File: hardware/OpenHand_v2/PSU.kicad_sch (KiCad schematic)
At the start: 23 parts, among them Q1 AO3401A, U2 TPS565201DDCR, U3 AMS1117-3.3

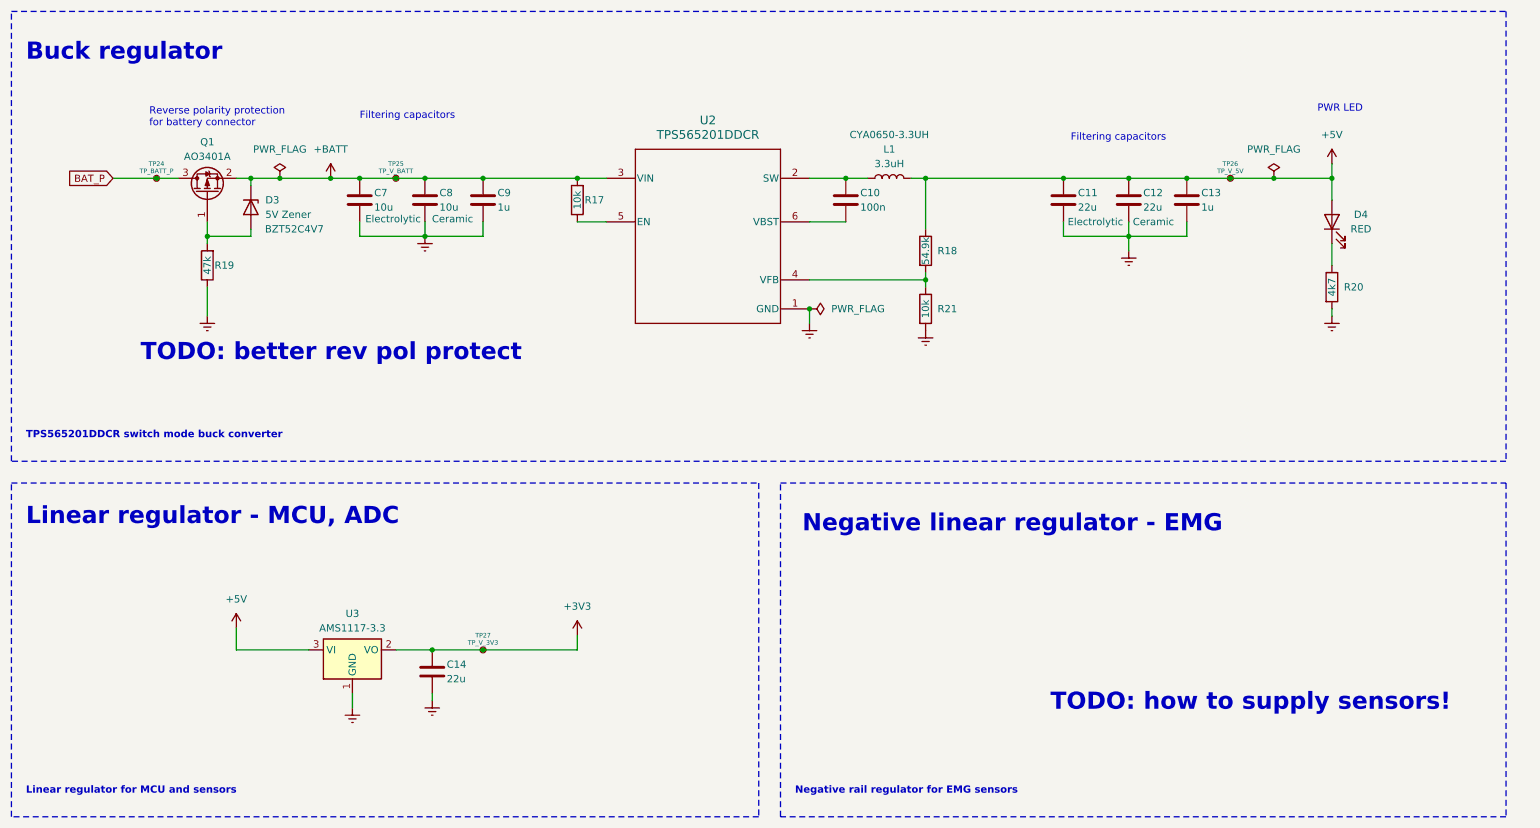
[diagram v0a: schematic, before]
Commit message: Update V2 schematic and start PCB layout
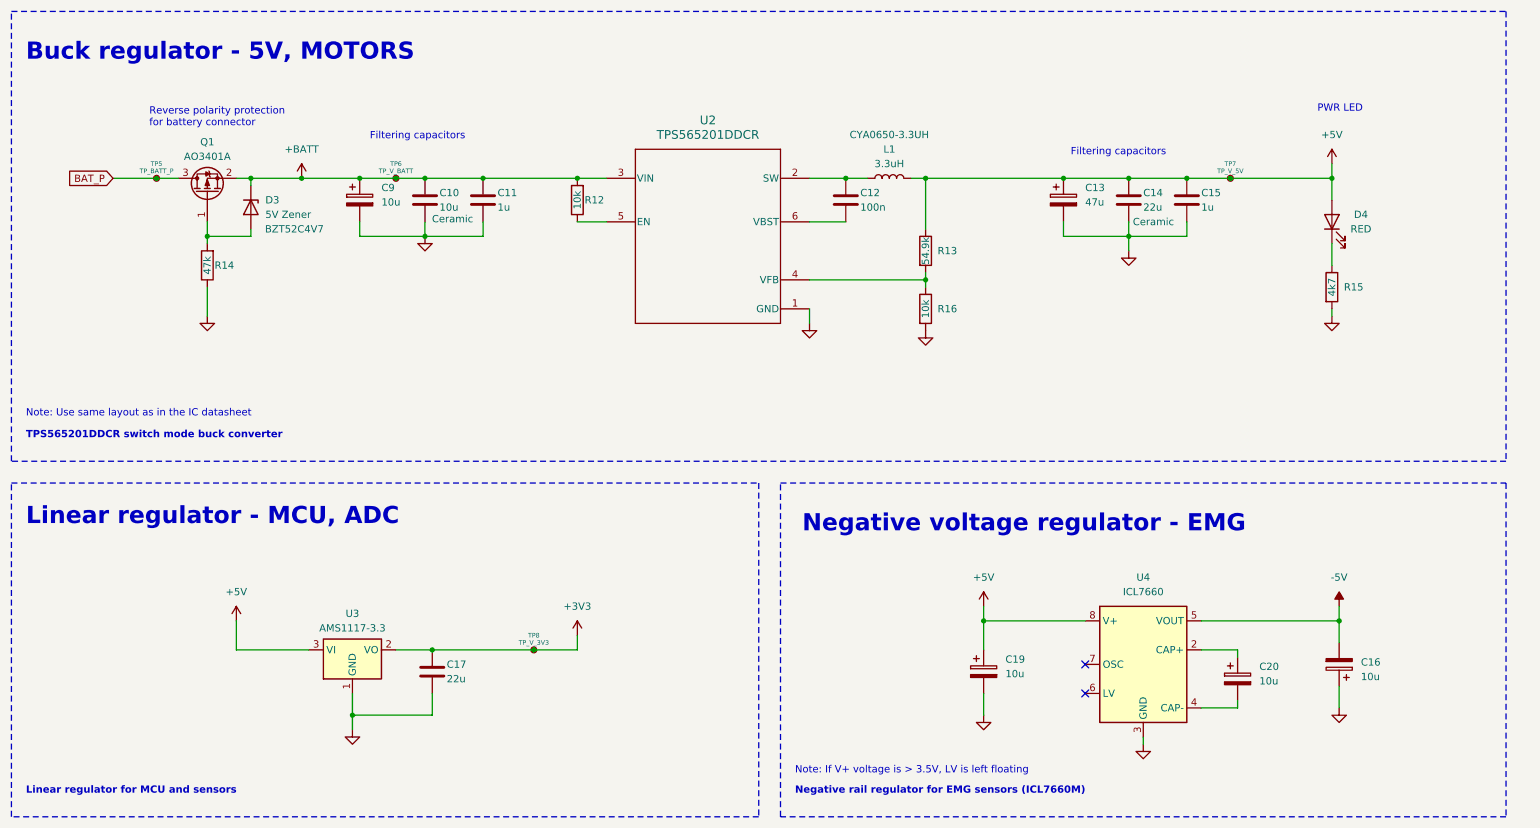
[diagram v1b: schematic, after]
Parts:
- removed C11: 22u, Capacitor_SMD:C_0805_2012Metric, symbol Device:C
- removed C7: 10u, Capacitor_SMD:C_0805_2012Metric, symbol Device:C
- added C13: 47u, Capacitor_SMD:CP_Elec_6.3x5.4, symbol Device:C_Polarized
- added C16, C19, C20, C9: 10u, Capacitor_SMD:CP_Elec_4x5.4, symbol Device:C_Polarized
- added U4: ICL7660, Package_SO:MSOP-8_3x3mm_P0.65mm, symbol Regulator_SwitchedCapacitor:ICL7660
- renumbered C8 to C10, C9 to C11, C10 to C12, C12 to C14, C13 to C15, C14 to C17, R17 to R12, R18 to R13, R19 to R14, R20 to R15, R21 to R16, TP24 to TP5, TP25 to TP6, TP26 to TP7, TP27 to TP8
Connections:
- net +5V: now also C13.1, C19.1, U4.8 (V+)
- net +BATT: now also C9.1
- net Earth renamed GND
- net GND: now also C13.2, C16.1, C19.2, C9.2, U4.3 (GND)
- new net: C20.1, U4.2 (CAP+)
- new net: C20.2, U4.4 (CAP-)
- new net -5V: C16.2, U4.5 (VOUT)
- no-connect marks 0 -> 2
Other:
- note added: "Buck regulator - 5V, MOTORS"
- note added: "Negative rail regulator for EMG sensors (ICL7660M)"
- note added: "Negative voltage regulator - EMG"
- note added: "Note: If V+ voltage is > 3.5V, LV is left floating"
- note added: "Note: Use same layout as in the IC datasheet"
- note removed: "Buck regulator"
- note removed: "Negative linear regulator - EMG"
- note removed: "Negative rail regulator for EMG sensors"
- note removed: "TODO: better rev pol protect"
- note removed: "TODO: how to supply sensors!"
- moved on the sheet: TP8

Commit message: Add V2 PCB and update CubeIDE config for V2
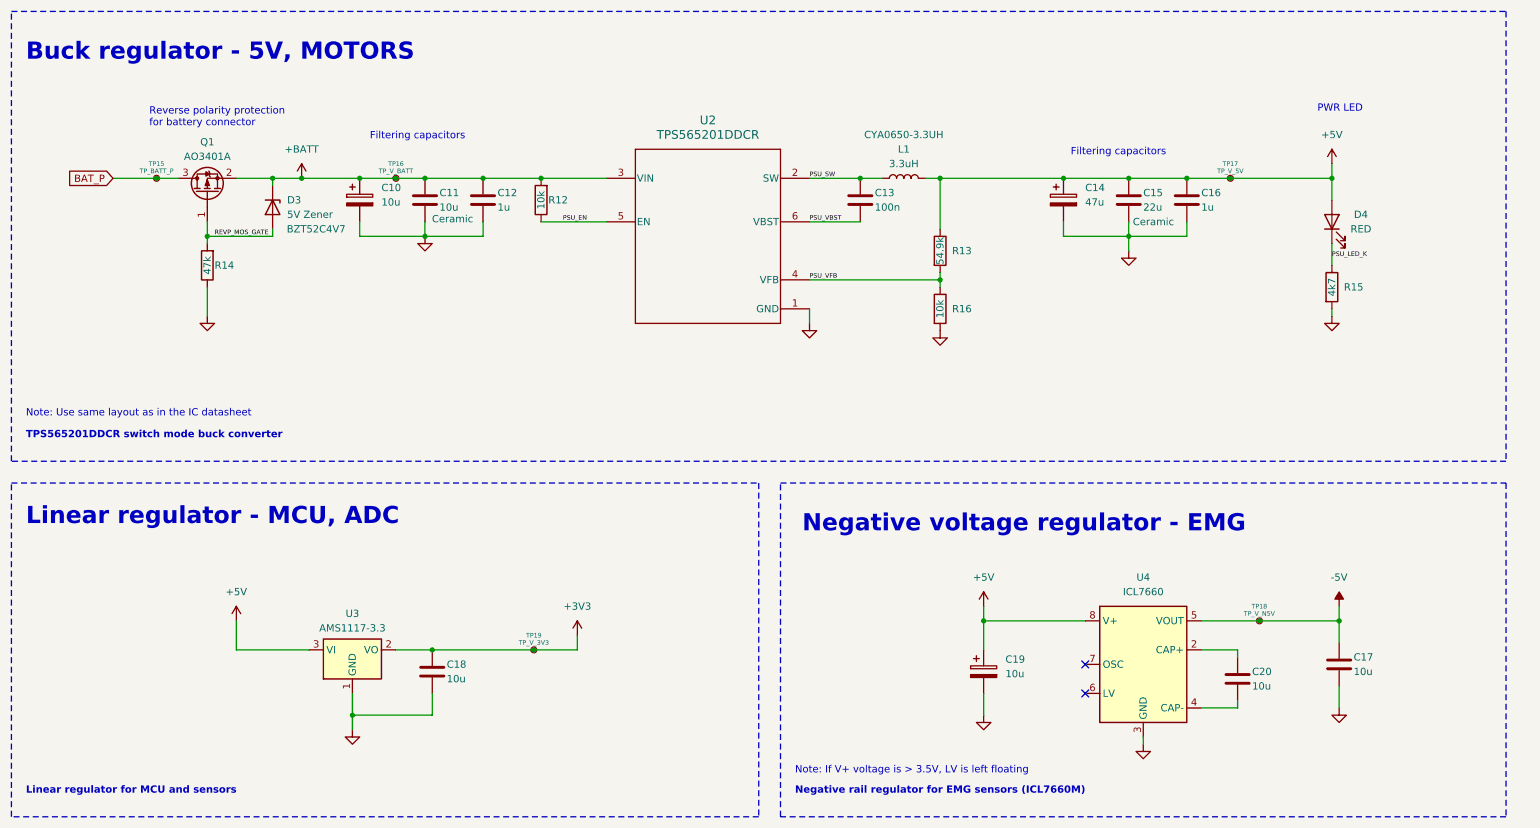
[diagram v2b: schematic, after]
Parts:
- removed C16, C20: 10u, Capacitor_SMD:CP_Elec_4x5.4, symbol Device:C_Polarized
- added C17, C20: 10u, Capacitor_SMD:C_0805_2012Metric, symbol Device:C
- added TP18: TP_V_N5V, TestPoint:TestPoint_Pad_D2.0mm, symbol Connector:TestPoint_Small
- C18: renamed from C17; value 22u -> 10u
- TP17: renamed from TP7; footprint TestPoint:TestPoint_Pad_D1.0mm -> TestPoint:TestPoint_Pad_D2.0mm
- TP19: renamed from TP8; footprint TestPoint:TestPoint_Pad_D1.0mm -> TestPoint:TestPoint_Pad_D2.0mm
- renumbered C9 to C10, C10 to C11, C11 to C12, C12 to C13, C13 to C14, C14 to C15, C15 to C16, TP5 to TP15, TP6 to TP16
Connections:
- net -5V: now also C17.1, TP18.1
- net GND: now also C17.2
- net REVP_MOS_GATE: now reaches D3.2 (A), Q1.1 (G), R14.2
- net PSU_SW: now reaches C13.1, L1.1, U2.2 (SW)
- net PSU_VFB: now reaches R13.2, R16.1, U2.4 (VFB)
- net PSU_EN: now reaches R12.1, U2.5 (EN)
- net PSU_VBST: now reaches C13.2, U2.6 (VBST)
- net at U4.2 (CAP+): now also C20.1
- net at U4.4 (CAP-): now also C20.2
- net PSU_LED_K: now reaches D4.1 (K), R15.1
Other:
- moved on the sheet: C13, D3, L1, R12, R13, R16

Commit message: EMG sensor quickfix, upadte ADC and DMA config
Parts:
- U4: footprint Package_SO:MSOP-8_3x3mm_P0.65mm -> Package_SO:SOP-8_3.9x4.9mm_P1.27mm
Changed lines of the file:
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@@
 			)
 		)
-		(property "Footprint" "Package_SO:MSOP-8_3x3mm_P0.65mm"
+		(property "Footprint" "Package_SO:SOP-8_3.9x4.9mm_P1.27mm"
 			(at 218.44 135.89 0)
 			(effects
